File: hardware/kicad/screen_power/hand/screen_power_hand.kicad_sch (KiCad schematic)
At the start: 8 parts, among them J2 GPIO17 / GND, Q1 2N3904, Q2 2N3906

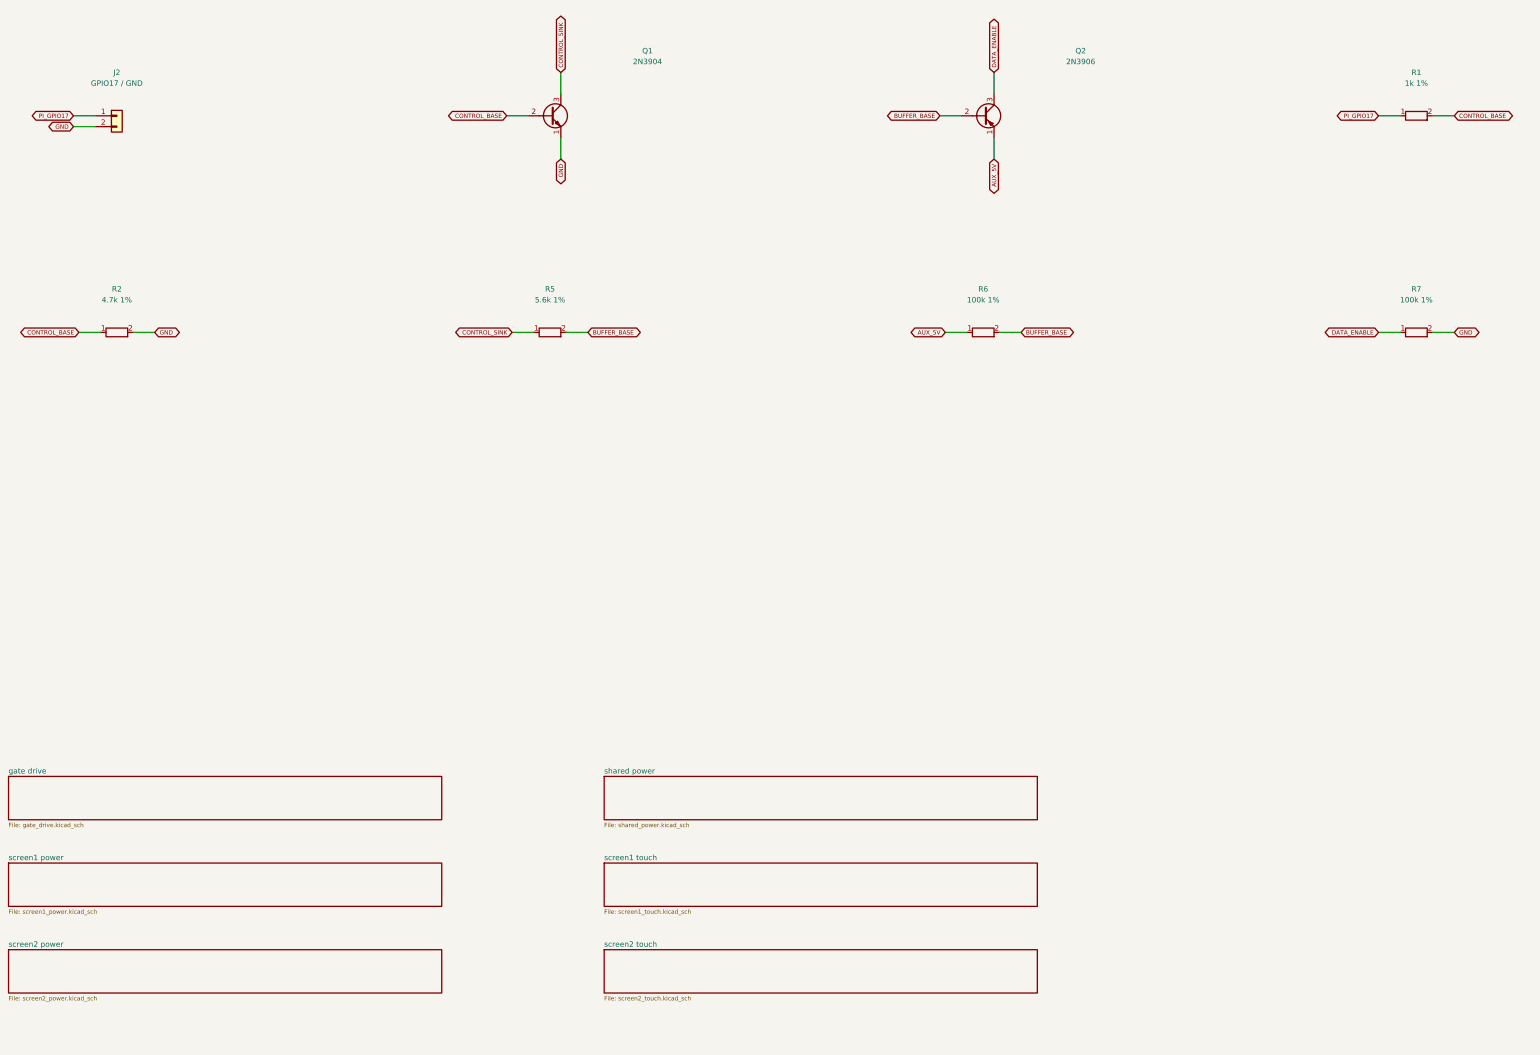
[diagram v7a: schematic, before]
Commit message: feat(hardware): lower screen power cost and finish copper contours
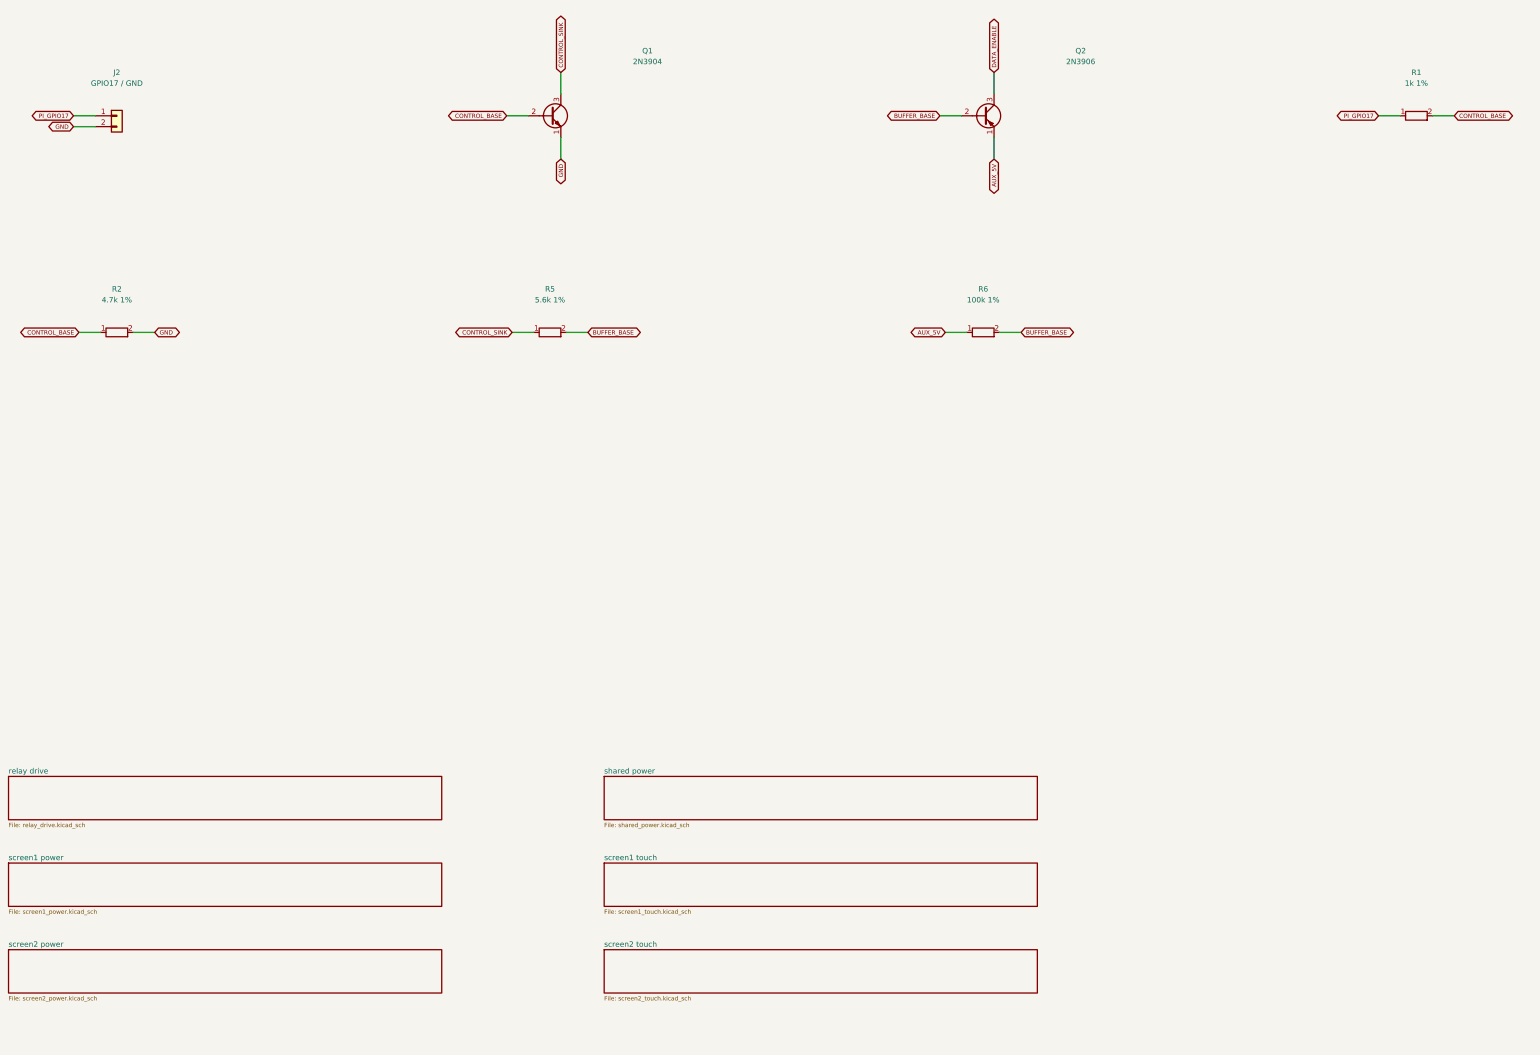
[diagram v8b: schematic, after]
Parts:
- removed R7: 100k 1%, Resistor_THT:R_Axial_DIN0207_L6.3mm_D2.5mm_P10.16mm_Horizontal, symbol screen_symbols:Device_R
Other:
- removed sheet gate drive
- added sheet relay drive (relay_drive.kicad_sch)
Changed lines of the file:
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@@
   (title_block
     (title "Segno screen power / hand / control")
-    (rev "M prototype")
-    (comment 1 "AUX-powered relays; each host VBUS supplies only its presence detector.")
-    (comment 2 "Physical verification required before release."))
+    (rev "N prototype")
+    (comment 1 "One normally open contact switches AUX; every board load sits behind F1.")
+    (comment 2 "AUX-powered relays; each host VBUS supplies only its presence detector.")
+    (comment 3 "Physical verification required before release."))
   (wire
     (pts
@@
         (path "/63a63dd8-c505-5bb8-8418-5eb0e558e546"
           (reference "R6")
-          (unit 1)))))
-  (wire
-    (pts
-      (xy 351.79 114.3)
-      (xy 346.71 114.3))
-    (stroke
-      (width 0)
-      (type default))
-)
-  (global_label "DATA_ENABLE"
-    (shape bidirectional)
-    (at 346.71 114.3 180)
-    (effects
-      (font
-        (size 1.0 1.0))
-      (justify right))
-)
-  (wire
-    (pts
-      (xy 359.41 114.3)
-      (xy 364.49 114.3))
-    (stroke
-      (width 0)
-      (type default))
-)
-  (global_label "GND"
-    (shape bidirectional)
-    (at 364.49 114.3 0)
-    (effects
-      (font
-        (size 1.0 1.0))
-      (justify left))
-)
-  (symbol
-    (lib_id "screen_symbols:Device_R")
-    (at 355.59999999999997 114.3 90)
-    (unit 1)
-    (in_bom yes)
-    (on_board yes)
-    (dnp no)
-    (property "Reference" "R7"
-      (at 355.59999999999997 104.14 90)
-      (effects
-        (font
-          (size 1.27 1.27))))
-    (property "Value" "100k 1%"
-      (at 355.59999999999997 106.68 90)
-      (effects
-        (font
-          (size 1.27 1.27))))
-    (property "Footprint" "Resistor_THT:R_Axial_DIN0207_L6.3mm_D2.5mm_P10.16mm_Horizontal"
-      (at 355.59999999999997 114.3 90)
-      (effects
-        (font
-          (size 1.27 1.27))
-        (hide yes)))
-    (property "MPN" "MFR-25FBF52-100K"
-      (at 355.59999999999997 114.3 90)
-      (effects
-        (font
-          (size 1.27 1.27))
-        (hide yes)))
-    (pin "1"
-)
-    (pin "2"
-)
-    (instances
-      (project "screen_power_hand"
-        (path "/63a63dd8-c505-5bb8-8418-5eb0e558e546"
-          (reference "R7")
           (unit 1)))))
   (sheet
@@
     (fill
       (color 0 0 0 0))
-    (property "Sheetname" "gate drive"
+    (property "Sheetname" "relay drive"
       (at 25.4 217.17 0)
       (effects
@@
           (size 1.27 1.27))
         (justify left)))
-    (property "Sheetfile" "gate_drive.kicad_sch"
+    (property "Sheetfile" "relay_drive.kicad_sch"
       (at 25.4 229.87 0)
       (effects
